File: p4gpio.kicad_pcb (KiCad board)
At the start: 4 copper layers, 88.9 x 22.9 mm, 90 parts, among them J1 C2760486, J10 Conn_01x04_Socket, J2 C2760486, J3 Conn_01x08_Pin, J4 Conn_01x08_Pin, J5 Conn_01x08_Pin, J6 Conn_01x08_Pin, J7 Conn_01x08_Pin, J8 Conn_01x08_Pin, J9 Conn_01x04_Socket, Q1 MBT3906DW1, Q2 AO3401A, Q3 MBT3906DW1, Q4 AO3401A, U1 TLV62569DBV, U3 W25Q128JVS, U4 TLV62569DBV, Y1 40MHz(+-10 ppm) C501798

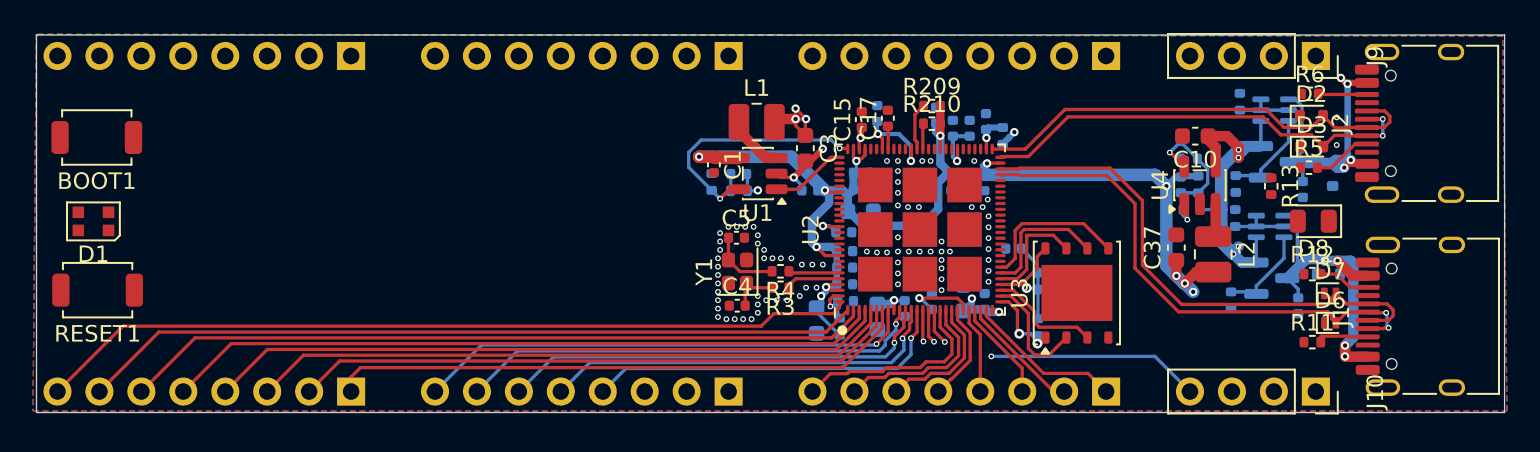
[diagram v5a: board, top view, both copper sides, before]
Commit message: Fix bootstrapping pins. Start fixing DRC
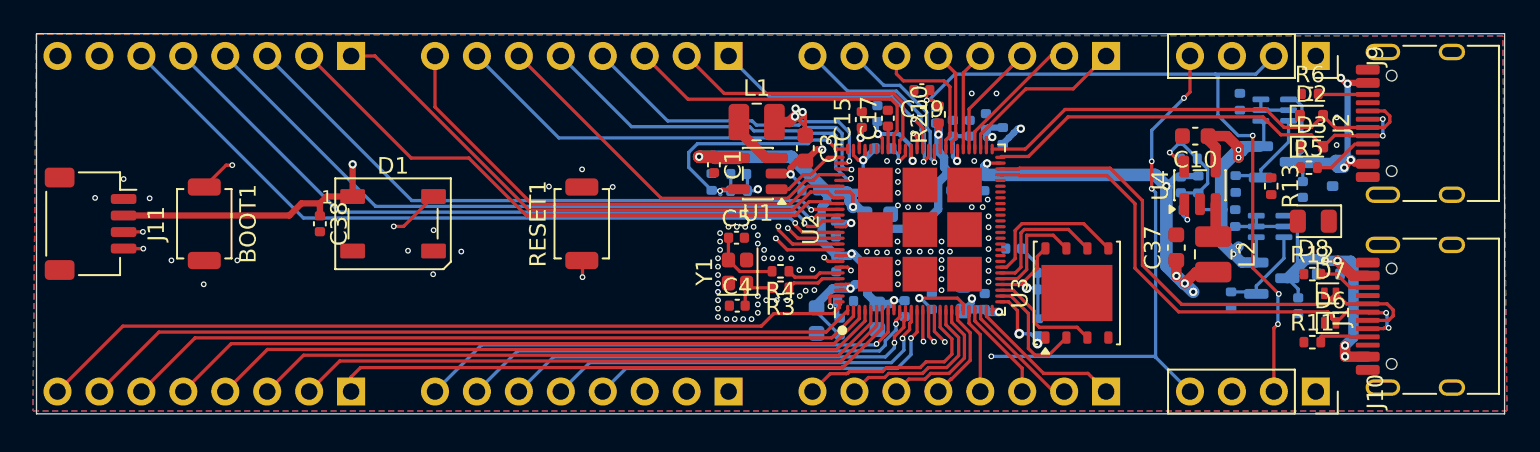
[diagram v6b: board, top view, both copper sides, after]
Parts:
- added C38: 0.1uF, Capacitor_SMD:C_0402_1005Metric, F.Cu at (139.8, 84.3)
- added C39: 0.1uF, Capacitor_SMD:C_0402_1005Metric, F.Cu at (176.3, 76.2)
- added J11: Conn_01x04, Connector_JST:JST_SH_SM04B-SRSS-TB_1x04-1MP_P1.00mm_Horizontal, F.Cu at (126.0, 84.3)
- D1: value WS2812B-2020 -> WS2812B; footprint LED_SMD:LED_WS2812B-2020_PLCC4_2.0x2.0mm -> LED_SMD:LED_WS2812B_PLCC4_5.0x5.0mm_P3.2mm
- R209: value 10k -> 10K; moved to B.Cu
- R210: value 10k -> 10K
- moved RESET1 29.6 mm to (155.7, 84.3), turned to 90 degrees
- moved D1 18.1 mm to (144.3, 84.3), turned to 0 degrees
- moved BOOT1 8.35 mm to (132.8, 84.3), turned to -90 degrees
- moved R209 3.89 mm to (174.0, 79.8)
- moved C7 1.85 mm to (173.5, 87.0)
- moved C12 1.85 mm to (173.5, 88.0)
- moved C14 1.06 mm to (173.6, 83.7)
- moved C6 0.92 mm to (171.1, 86.7), turned to -90 degrees
- moved C13 0.84 mm to (173.5, 82.4)
- moved C16 0.84 mm to (173.5, 81.4)
- moved R210 0.69 mm to (177.3, 77.7), turned to 90 degrees
- moved C8 0.52 mm to (171.1, 84.6), turned to -90 degrees
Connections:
- D1 pad 1: unconnected-(D1-DOUT-Pad1) -> +3.3V
- D1 pad 2: GND -> unconnected-(D1-DOUT-Pad2)
- D1 pad 3: /NEOPIXEL -> GND
- D1 pad 4: +3.3V -> /NEOPIXEL
- R209 pad 1: /Minimal P4 V3/GPIO35 -> +3.3V
- R209 pad 2: +3.3V -> /GPIO36
- R210 pad 1: /BOOT -> +3.3V
- R210 pad 2: +3.3V -> /BOOT
- U2 pad 65: /BOOT -> /T2_7
- U2 pad 66: /Minimal P4 V3/GPIO35 -> /BOOT
- U2 pad 68: /T2_7 -> /GPIO36
- U2 pad 95: /Minimal P4 V3/GPIO52/ADC -> /NEOPIXEL
- U2 pad 97: /Minimal P4 V3/GPIO53/ADC -> /SDA
- U2 pad 98: /Minimal P4 V3/GPIO54/ADC -> /SCL
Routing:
- net /BOOT: track 1.56 -> 94.9 mm, vias 0 -> 6
- net /T1_0: track 0.00 -> 52.2 mm, vias 0 -> 1
- net /T1_1: track 0.00 -> 49.6 mm, vias 0 -> 1
- net /SCL: track 0.00 -> 49.4 mm, vias 0 -> 2
- net /SDA: track 0.00 -> 48.8 mm, vias 0 -> 2
- net /T1_2: track 0.00 -> 48.4 mm, vias 0 -> 1
- net +3.3V: track 111.1 -> 159.0 mm
- net /T1_3: track 0.00 -> 44.2 mm, vias 0 -> 1
- net /T1_4: track 0.00 -> 41.4 mm, vias 0 -> 1
- net /T1_5: track 0.00 -> 38.5 mm, vias 0 -> 1
- net /RESET: track 26.7 -> 64.7 mm, vias 2 -> 6
- net /T1_6: track 0.00 -> 36.5 mm
- net /T1_7: track 0.00 -> 34.0 mm
- net /NEOPIXEL: track 0.00 -> 31.6 mm, vias 0 -> 2
- net /T2_0: track 0.00 -> 30.5 mm
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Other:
- board size 88.9 x 22.9 mm -> 88.9 x 23 mm

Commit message: Done?
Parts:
- added G***: LOGO, chickadee:chickadee_1mm_fcu, F.Cu at (144.5, 81.0)
- J1, J2: footprint Connector_USB:USB_C_Receptacle_HRO_TYPE-C-31-M-12 -> Adafruit:USB_C_Receptacle_HRO_TYPE-C-31-M-31
- moved R13 2.54 mm to (197.6, 84.6), turned to 90 degrees
- moved R6 2.08 mm to (201.7, 77.2), turned to 90 degrees
- moved C39 0.28 mm to (176.0, 76.2)
- moved D8 0.09 mm to (200.0, 84.1)
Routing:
- net /HS_VBUS: track 20.1 -> 22.4 mm
- net VBUS: track 27.9 -> 30.0 mm, vias 4 -> 5
- net /FS_VBUS: track 18.4 -> 19.8 mm
- net Net-(D8-A): track 0.00 -> 1.46 mm
- net Net-(J2-CC1): track 2.87 -> 3.99 mm
- net Net-(J2-CC2): track 3.01 -> 2.02 mm
- net GND: track 4.88 -> 5.65 mm, vias 92 -> 138
- added copper zone on F.Cu, net /HS_VBUS
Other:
- board size 88.9 x 23 mm -> 87.9 x 23 mm
- board text added: "0"
- board text added: "1"
- board text added: "2"
- board text added: "3"
- board text added: "3V"
- board text added: "4"
- board text added: "5"
- board text added: "6"
- board text added: "7"
- board text added: "Adafruit P4GPIO v1"
- board text added: "B"
- board text added: "B1"
- board text added: "B2"
- board text added: "B3"
- board text added: "Boot"
- board text added: "G"
- board text added: "NEOPIXEL:52"
- board text added: "R"
- board text added: "Reset"
- board text added: "SDA:53 SCL:54"
- board text added: "T1"
- board text added: "T2"
- board text added: "T3"

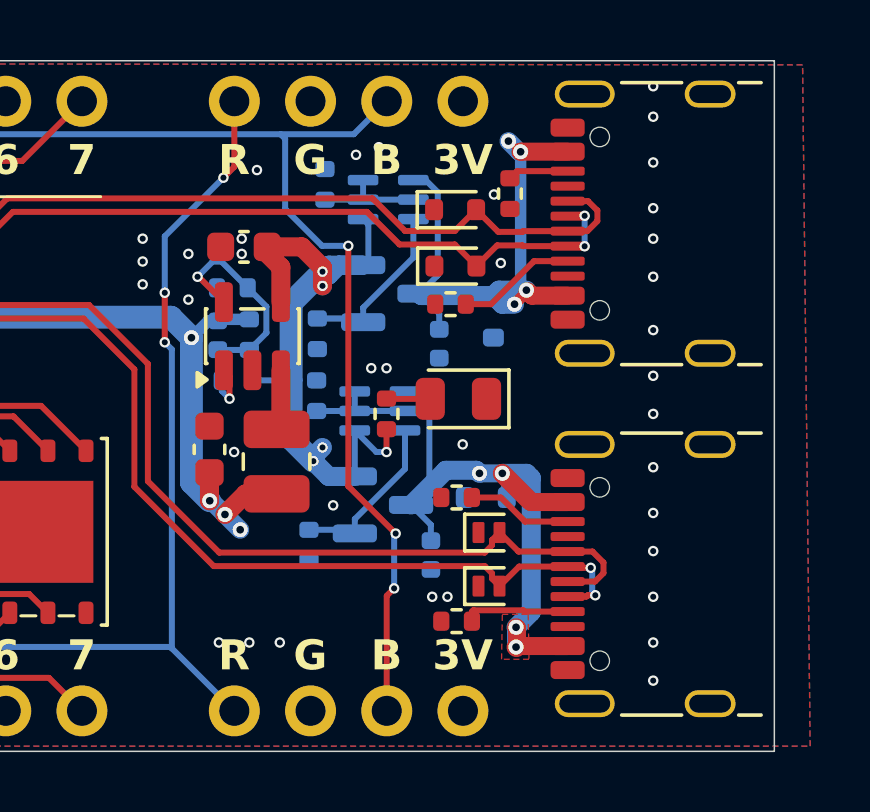
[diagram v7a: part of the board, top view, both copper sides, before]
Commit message: Prep to order. Need to make vias bigger
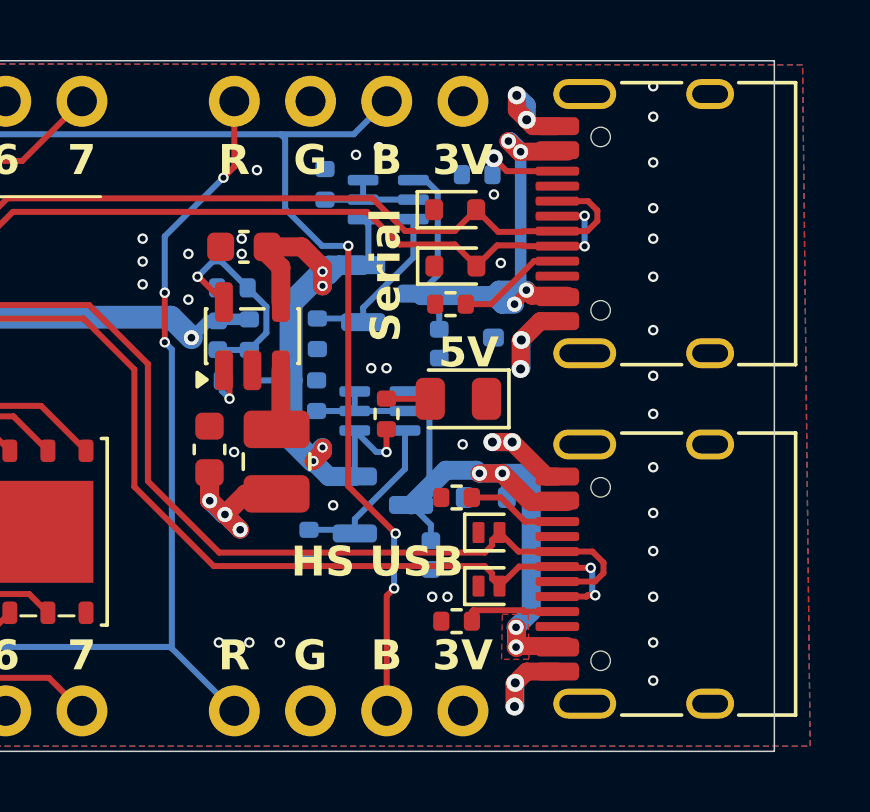
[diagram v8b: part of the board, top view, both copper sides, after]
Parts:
- C4, C5: value TODO -> 12pF
- J1, J2: footprint Adafruit:USB_C_Receptacle_HRO_TYPE-C-31-M-31 -> Connector_USB:USB_C_Receptacle_HRO_TYPE-C-31-M-12
- R13: value 5.1K(1%) -> 2.2K
- R6: moved to B.Cu
- moved R6 1.26 mm to (200.6, 76.6), turned to 0 degrees
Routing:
- net GND: track 5.65 -> 18.5 mm, vias 138 -> 146
- net +3.3V: track 159.0 -> 161.8 mm
- net Net-(J2-CC2): track 2.02 -> 3.20 mm, vias 0 -> 1
- net /HS_VBUS: track 22.4 -> 23.1 mm
- net VBUS: track 30.0 -> 30.6 mm
- net /FS_VBUS: track 19.8 -> 20.4 mm
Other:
- board text added: "5V"
- board text added: "HS USB"
- board text added: "Serial"
